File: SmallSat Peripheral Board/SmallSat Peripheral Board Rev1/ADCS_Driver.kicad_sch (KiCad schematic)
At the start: 0 parts

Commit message: Peripheral Board Rev 1 Complete
Time to test!
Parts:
- added C14, C15, C16: C, symbol Device:C
- added L3: Phase A, symbol Device:L
- added L4: Phase B, symbol Device:L
- added L5: Phase C, symbol Device:L
- added R16, R17, R18, R19: 10k, symbol Device:R
- added R20, R21, R22: 1k, symbol Device:R
- added U10: L293D, Package_DIP:DIP-16_W7.62mm, symbol Driver_Motor:L293D
- added U7, U8, U9: LM339, symbol Comparator:LM339
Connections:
- new net: L3.2, L4.2, L5.2
- new net: R20.1, U7.5 (+)
- new net: R16.2, U10.1 (EN1,2)
- new net: R21.1, U8.5 (+)
- new net: R22.1, U9.5 (+)
- new net +5V: R16.1, U10.16 (VCC1)
- new net 7.4V: U10.8 (VCC2)
- new net Control1: U10.2 (1A)
- new net Control2: U10.7 (2A)
- new net Control3: U10.10 (3A)
- new net GND: C14.2, C15.2, C16.2, U10.12 (GND), U10.13 (GND), U10.4 (GND), U10.5 (GND)
- new net Neutral: R17.1, R18.1, R19.1, U7.4 (-), U8.4 (-), U9.4 (-)
- new net Phase A: C14.1, L3.1, R19.2, R20.2, U10.3 (1Y)
- new net Phase A Bemf: U7.2
- new net Phase B: C15.1, L4.1, R18.2, R21.2, U10.6 (2Y)
- new net Phase B Bemf: U8.2
- new net Phase C: C16.1, L5.1, R17.2, R22.2, U10.11 (3Y)
- new net Phase C Bemf: U9.2

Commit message: ADCS Driver Work
Nothing final yet
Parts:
- removed R16: 10k, symbol Device:R
- removed U10: L293D, Package_DIP:DIP-16_W7.62mm, symbol Driver_Motor:L293D
- C14, C15, C16: value C -> 470n

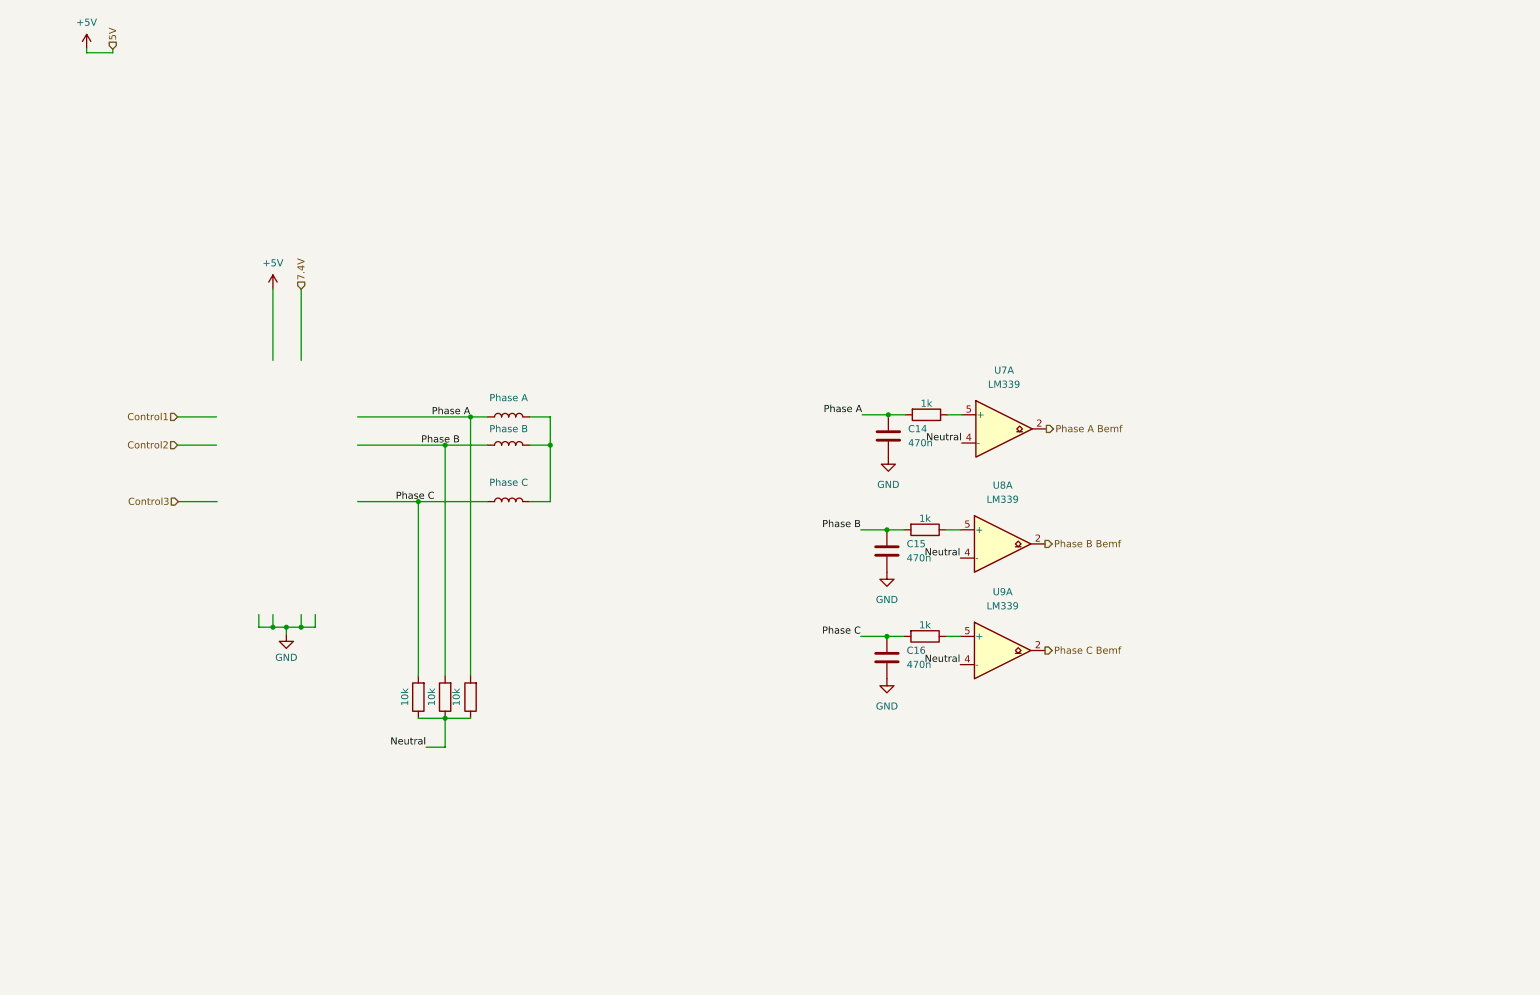
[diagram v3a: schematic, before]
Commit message: ADCS Driver Rev 2
- Redesigned the ESC with modern ICs that have bootstrapping infrastructure
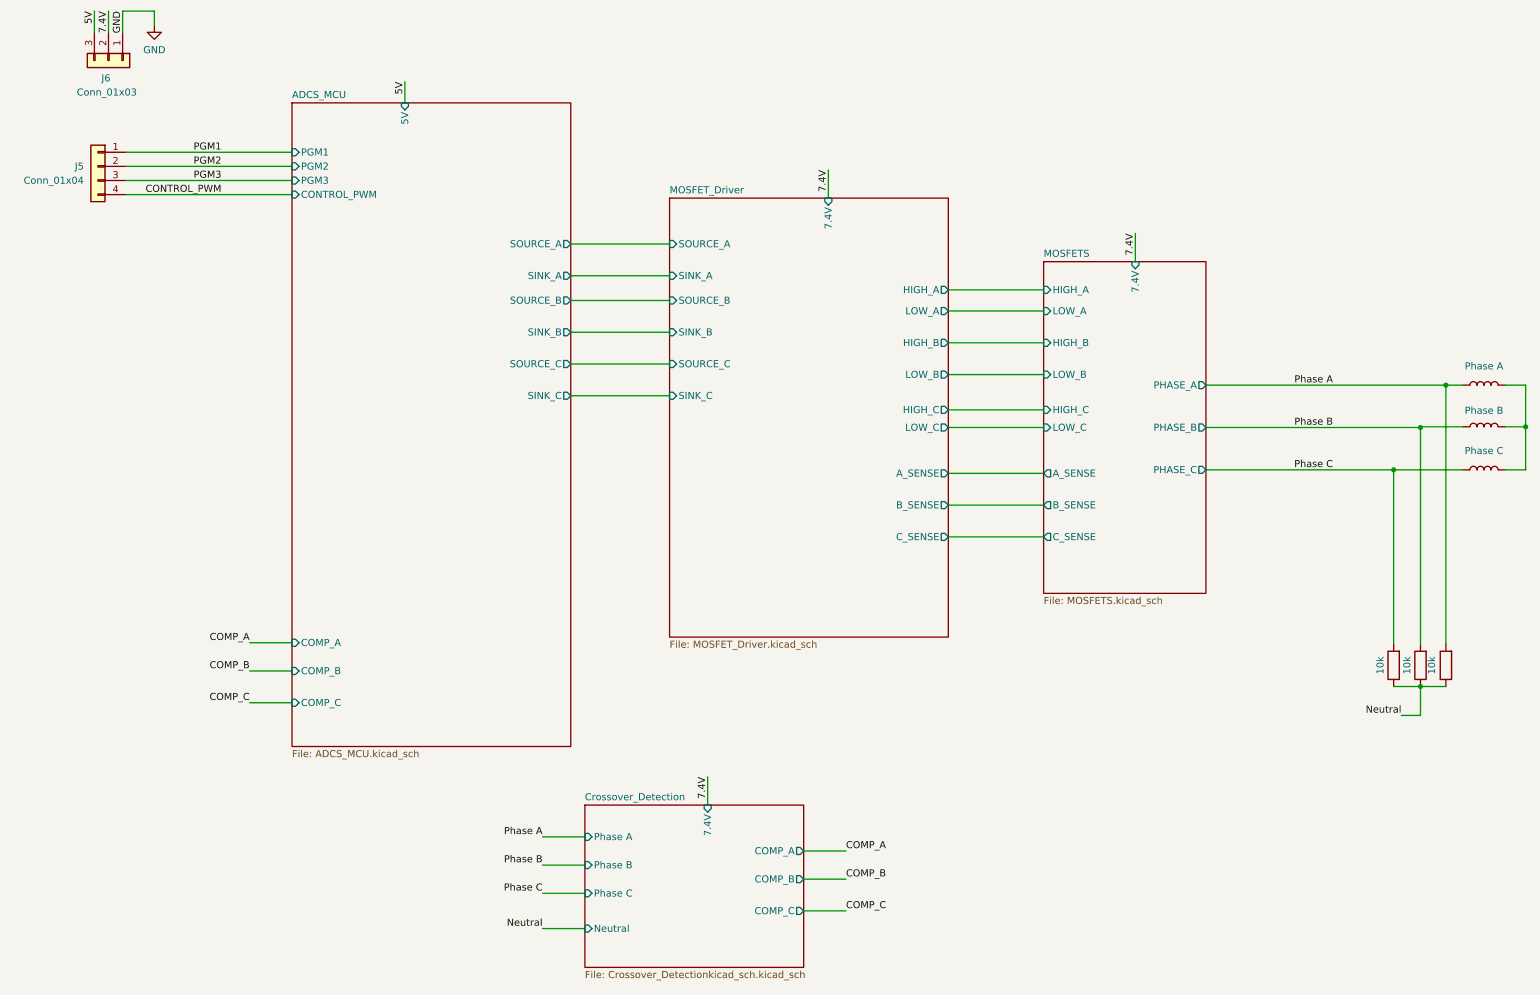
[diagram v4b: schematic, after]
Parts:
- removed C14, C15, C16: 470n, symbol Device:C
- removed R20, R21, R22: 1k, symbol Device:R
- removed U7, U8, U9: LM339, symbol Comparator:LM339
- added J5: Conn_01x04, symbol Connector_Generic:Conn_01x04
- added J6: Conn_01x03, symbol Connector_Generic:Conn_01x03
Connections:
- net 7.4V: now also J6.2 (Pin_2)
- net GND: now also J6.1 (Pin_1)
- new net 5V: J6.3 (Pin_3)
- new net CONTROL_PWM: J5.4 (Pin_4)
- new net PGM1: J5.1 (Pin_1)
- new net PGM2: J5.2 (Pin_2)
- new net PGM3: J5.3 (Pin_3)
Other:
- added sheet ADCS_MCU (ADCS_MCU.kicad_sch)
- added sheet Crossover_Detection (Crossover_Detectionkicad_sch.kicad_sch)
- added sheet MOSFETS (MOSFETS.kicad_sch)
- added sheet MOSFET_Driver (MOSFET_Driver.kicad_sch)

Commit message: Organized Repository
- Better overall file organization
- Included necessary documentation to be filled out
- Included KiCAD libraries
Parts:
- removed J5: Conn_01x04, symbol Connector_Generic:Conn_01x04
- removed J6: Conn_01x03, symbol Connector_Generic:Conn_01x03
